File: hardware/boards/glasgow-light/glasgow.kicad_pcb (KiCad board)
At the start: 2 copper layers, 90.2 x 21 mm, 183 parts, among them J1 USB_C_USB2.0, J10 AUX, J2 IDC-Header_2x5_P2.54mm, J3 IDC-Header_2x5_P2.54mm, J4 Conn_01x02, U1 LM358_DFN, U10 SN74LVC1T45DCKR, U11 SN74LVC1T45DCKR, U12 INA180A2, U15 TPD3S014, U16 SN74LVC1T45DCKR, U17 SN74LVC1T45DCKR, U18 SN74LVC1T45DCKR, U19 PCA6408APW, U2 GD32VF103T, U31 TPS73101DBV, U36 TLV73312PQDRVR, U4 SN74LVC1T45DCKR, U5 ICE40UP5K-SG48ITR, U6 SN74LVC1T45DCKR, U8 TLV75533PDRVR, U9 SN74LVC1T45DCKR, Y1 8M

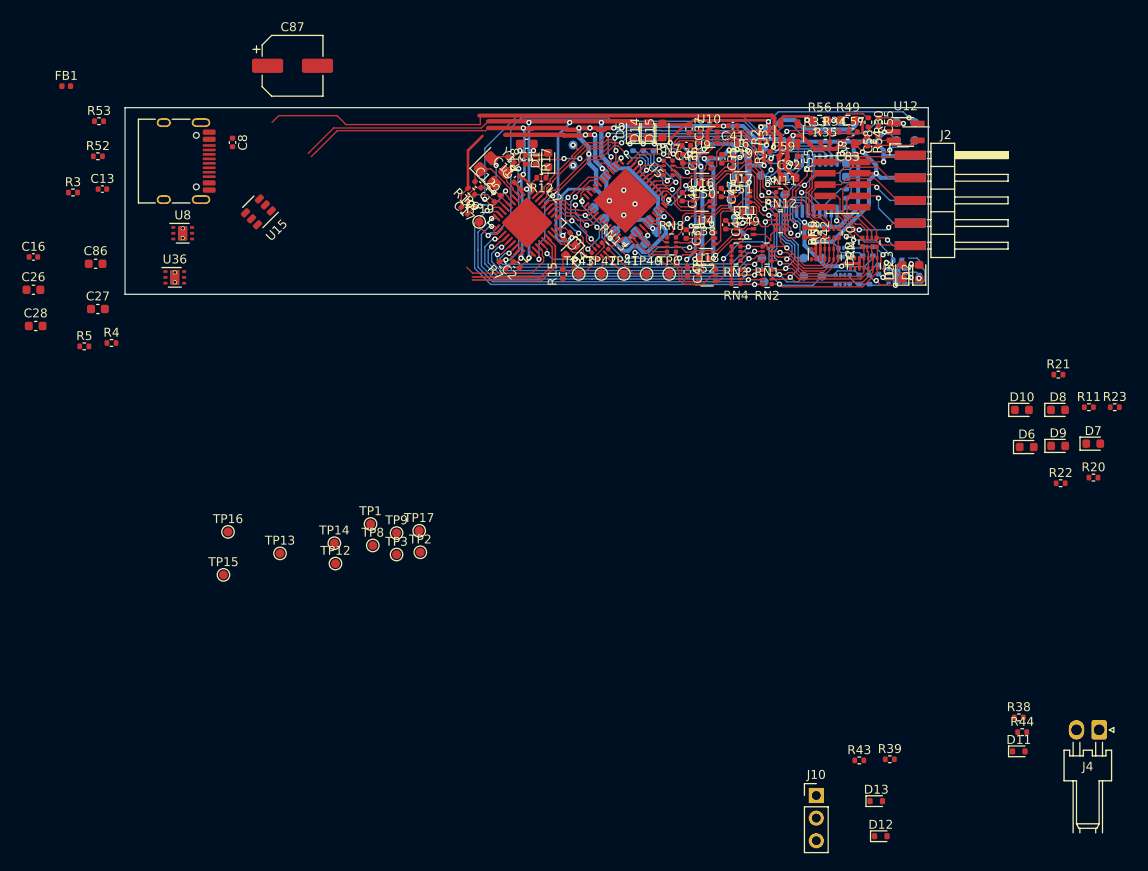
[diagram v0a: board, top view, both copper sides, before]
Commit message: replace SYNC and AUX connectors by test points
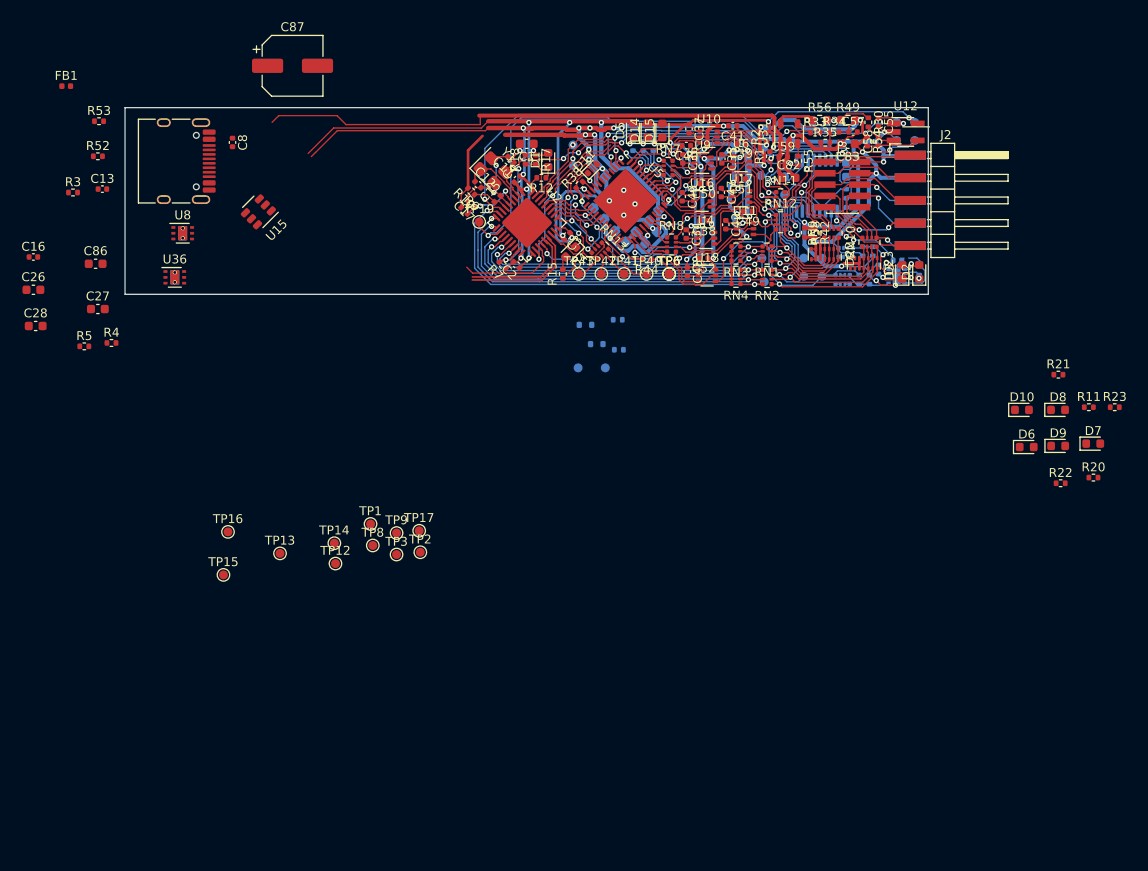
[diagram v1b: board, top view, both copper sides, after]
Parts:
- removed J10: AUX, Connector_PinHeader_2.54mm:PinHeader_1x03_P2.54mm_Vertical
- removed J4: Conn_01x02, Glasgow:Molex_KK-254_1x02_P2.54mm_Horizontal
- added TP18: SYNC, TestPoint:TestPoint_Pad_D1.0mm, B.Cu at (137.7, 62.9)
- added TP6: SYNC, TestPoint:TestPoint_Pad_D1.0mm, F.Cu at (144.9, 52.3)
- added TP7: SYNC, TestPoint:TestPoint_Pad_D1.0mm, B.Cu at (134.7, 62.9)
- D12, D13, R39, R43: moved to B.Cu
- moved D11 81.1 mm to (136.3, 40.5), turned to 45 degrees
- moved R38 77.5 mm to (134.8, 42.3), turned to 45 degrees
- moved R44 67.8 mm to (142.4, 50.7), turned to 180 degrees
- moved D12 66.3 mm to (135.5, 58.0)
- moved D13 60.1 mm to (136.8, 60.2)
- moved R43 56.4 mm to (139.1, 57.5)
- moved R39 55.1 mm to (139.3, 60.8)
- moved D4 0.18 mm to (133.9, 49.9)
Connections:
- R38 pad 2: Net-(R38-Pad2) -> /~SYNC_INT
- R39 pad 2: Net-(R39-Pad2) -> /AUX1
- R43 pad 2: Net-(R43-Pad2) -> /AUX2
- TP6 pad 1: /~SYNC -> /IO_Banks/~SYNC
- U5 pad 10: /~SYNC -> /~SYNC_INT
- U5 pad 11: Net-(U5-Pad11) -> /AUX2
- U5 pad 9: Net-(U5-Pad9) -> /AUX1
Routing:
- net /IO_Banks/~SYNC: track 0.00 -> 20.4 mm, vias 0 -> 2
- net /~SYNC: track 17.6 -> 0.00 mm, vias 2 -> 0
- net +3V3: track 256.5 -> 260.4 mm
- net /~FPGA_RESET: track 12.6 -> 15.7 mm
- net GND: track 337.5 -> 340.4 mm, vias 34 -> 35
- net /FPGA_DONE: track 20.2 -> 22.9 mm
- net Net-(U5-Pad4): track 1.87 -> 0.00 mm
- net /~SYNC_INT: track 0.00 -> 1.33 mm
- net /SCL: track 44.1 -> 45.2 mm
- net /AUX1: track 0.00 -> 1.00 mm, vias 0 -> 1
- net /AUX2: track 0.00 -> 0.78 mm, vias 0 -> 1

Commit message: most components are placed
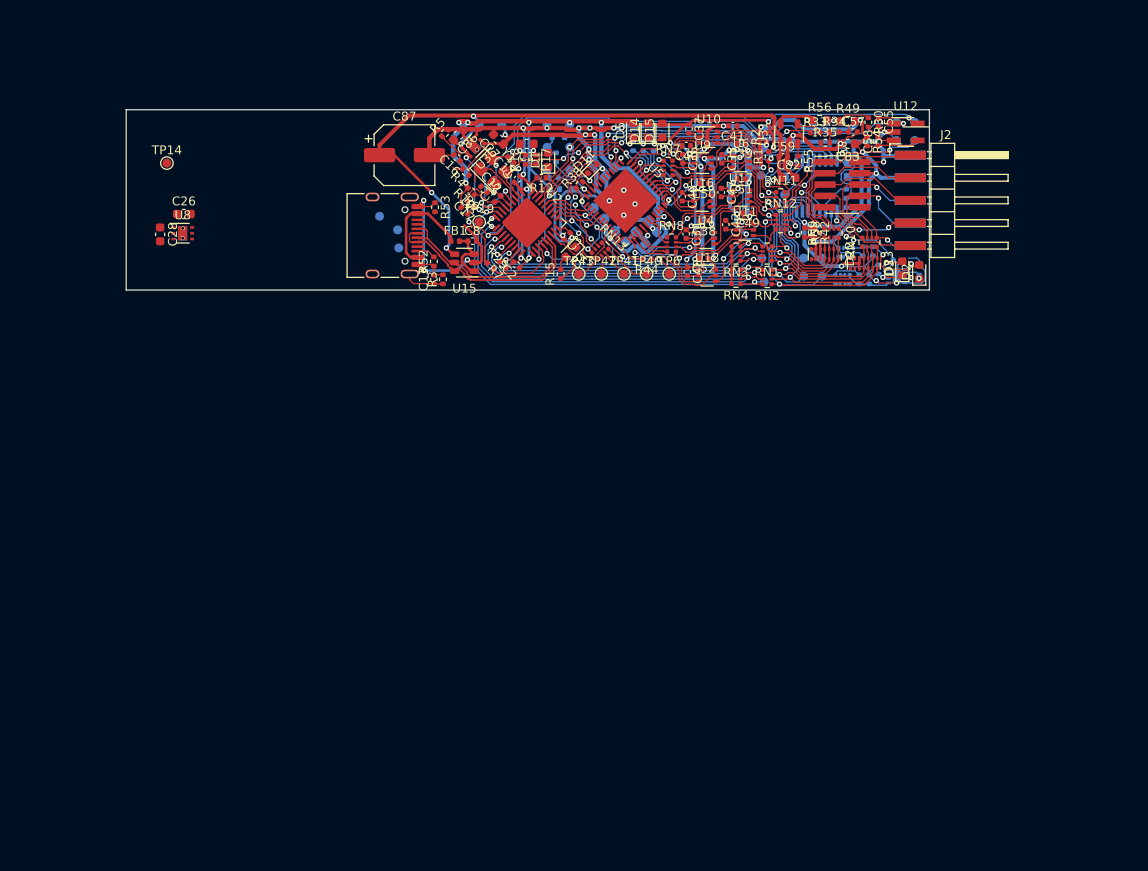
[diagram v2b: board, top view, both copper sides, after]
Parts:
- removed D10, D6: BLU, LED_SMD:LED_0603_1608Metric
- removed D7, D9: PNK, LED_SMD:LED_0603_1608Metric
- removed D8: WHT, LED_SMD:LED_0603_1608Metric
- removed R11, R23: 4k7, Resistor_SMD:R_0402_1005Metric
- removed R20, R22: 10k, Resistor_SMD:R_0402_1005Metric
- removed R21: 6k8, Resistor_SMD:R_0402_1005Metric
- removed TP17: 1V2, TestPoint:TestPoint_Pad_D1.0mm
- removed the TP6 at (144.9, 52.3)
- removed TP8: 5V, TestPoint:TestPoint_Pad_D1.0mm
- removed TP9: 3V3, TestPoint:TestPoint_Pad_D1.0mm
- added R29: 0, Resistor_SMD:R_0402_1005Metric, F.Cu at (124.8, 51.4)
- TP1, TP12, TP13, TP15, TP16, TP2, TP3: moved to B.Cu
- moved TP12 54.7 mm to (131.2, 35.6)
- moved TP3 52.0 mm to (133.7, 35.6)
- moved TP2 48.9 mm to (126.1, 35.6)
- moved C27 48.8 mm to (125.7, 37.2), turned to 135 degrees
- moved C16 48.8 mm to (121.1, 39.3), turned to 135 degrees
- moved R5 47.0 mm to (119.7, 36.5), turned to 45 degrees
- moved FB1 47.0 mm to (120.9, 48.6)
- moved TP14 46.6 mm to (88.5, 39.9)
- moved TP1 46.5 mm to (123.6, 35.6)
- moved R4 44.2 mm to (122.1, 40.9), turned to 135 degrees
- moved TP15 43.4 mm to (114.4, 47.4)
- moved C86 43.2 mm to (121.2, 36.7), turned to 225 degrees
- moved R3 42.7 mm to (119.5, 52.9), turned to 90 degrees
- moved R52 39.5 mm to (118.5, 50.9), turned to 90 degrees
- moved TP13 39.5 mm to (112.4, 45.8)
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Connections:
- net Net-(D12-Pad1) renamed /IO_Banks/AUX1~
- net Net-(D13-Pad1) renamed /IO_Banks/AUX2~
- U2 pad 21: +5V -> Net-(R29-Pad2)
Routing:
- net GND: track 340.4 -> 367.1 mm, vias 35 -> 39
- net +3V3: track 260.4 -> 240.7 mm, vias 23 -> 26
- net +5V: track 77.0 -> 91.2 mm, vias 0 -> 6
- net /xVBUS: track 0.00 -> 12.2 mm
- net /USB_P: track 13.5 -> 24.8 mm
- net +1V2: track 29.5 -> 39.9 mm, vias 4 -> 5
- net /USB_N: track 12.7 -> 22.8 mm
- net Net-(R29-Pad2): track 0.00 -> 8.26 mm
- net /VUSB: track 0.00 -> 6.57 mm
- net Net-(C16-Pad1): track 0.00 -> 5.87 mm
- net /AUX1: track 1.00 -> 5.91 mm
- net /SHLD: track 0.00 -> 4.57 mm
- net /AUX2: track 0.78 -> 4.22 mm
- net /IO_Banks/AUX2~: track 0.00 -> 2.74 mm
- net /IO_Banks/AUX1~: track 0.00 -> 2.66 mm
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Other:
- board size 90.2 x 21 mm -> 90.2 x 20.2 mm

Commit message: optimize
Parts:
- TP14, TP19: moved to B.Cu
- moved C28 34.6 mm to (122.3, 45.3), turned to 225 degrees
- moved U8 31.2 mm to (121.2, 43.2), turned to 225 degrees
- moved C26 30.2 mm to (120.3, 41.1), turned to 225 degrees
- moved TP14 27.7 mm to (116.2, 40.8)
- moved TP13 5.24 mm to (113.7, 40.8)
- moved TP16 4.93 mm to (119.4, 50.4)
- moved TP15 4.22 mm to (118.5, 48.5)
- moved TP19 2.62 mm to (126.0, 47.5)
- moved R9 1.90 mm to (120.8, 46.7)
- moved C17 1.78 mm to (124.0, 45.7), turned to 45 degrees
- moved R10 1.31 mm to (123.7, 43.9)
- moved R4 0.70 mm to (122.6, 41.4)
- moved C16 0.60 mm to (121.6, 39.6)
- moved C12 0.30 mm to (124.3, 43.1)
- moved C13 0.25 mm to (118.5, 52.7)
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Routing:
- net GND: track 367.1 -> 392.5 mm, vias 39 -> 42
- net +5V: track 91.2 -> 98.9 mm, vias 6 -> 7
- net /IO_Banks/VIOA: track 134.9 -> 127.6 mm
- net /xVBUS: track 12.2 -> 18.6 mm, vias 0 -> 1
- net Net-(C16-Pad1): track 5.87 -> 11.8 mm, vias 0 -> 2
- net /CC1: track 0.00 -> 4.19 mm, vias 0 -> 2
- net /USB_N: track 22.8 -> 25.7 mm, vias 0 -> 1
- net /NRST: track 7.06 -> 9.24 mm
- net /USB_P: track 24.8 -> 26.5 mm, vias 0 -> 1
- net +1V2: track 39.9 -> 41.1 mm
- net /VDDA: track 4.11 -> 3.01 mm
- net +3V3: track 240.7 -> 239.7 mm
- net VIO_CURRENT: track 61.4 -> 60.4 mm
- net /XTALIN: track 7.30 -> 7.99 mm
- net VIO_DAC: track 51.9 -> 51.3 mm
- added copper zone on B.Cu, net +5V
- added copper zone on F.Cu, net +5V
- added copper zone on F.Cu, net /SHLD
- added copper zone on B.Cu, net GND
- added copper zone on F.Cu, net GND
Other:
- board size 90.2 x 20.2 mm -> 63.9 x 20.2 mm

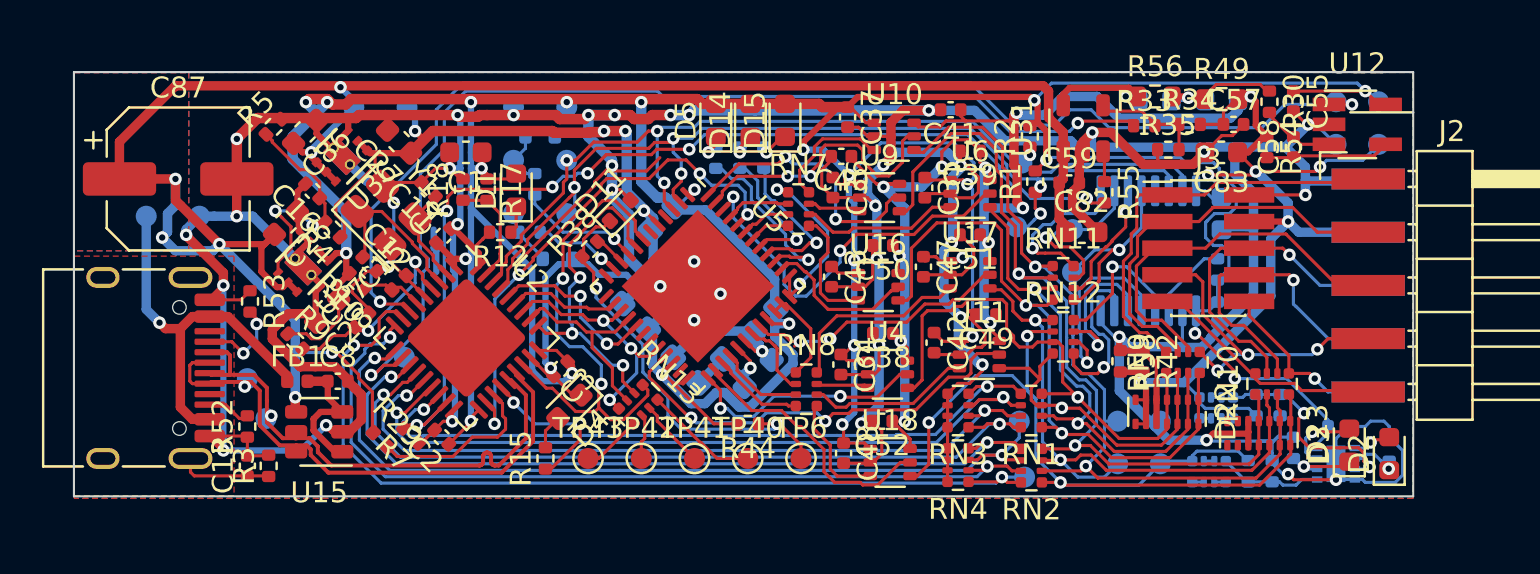
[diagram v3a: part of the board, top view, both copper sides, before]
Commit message: make the board a bit smaller
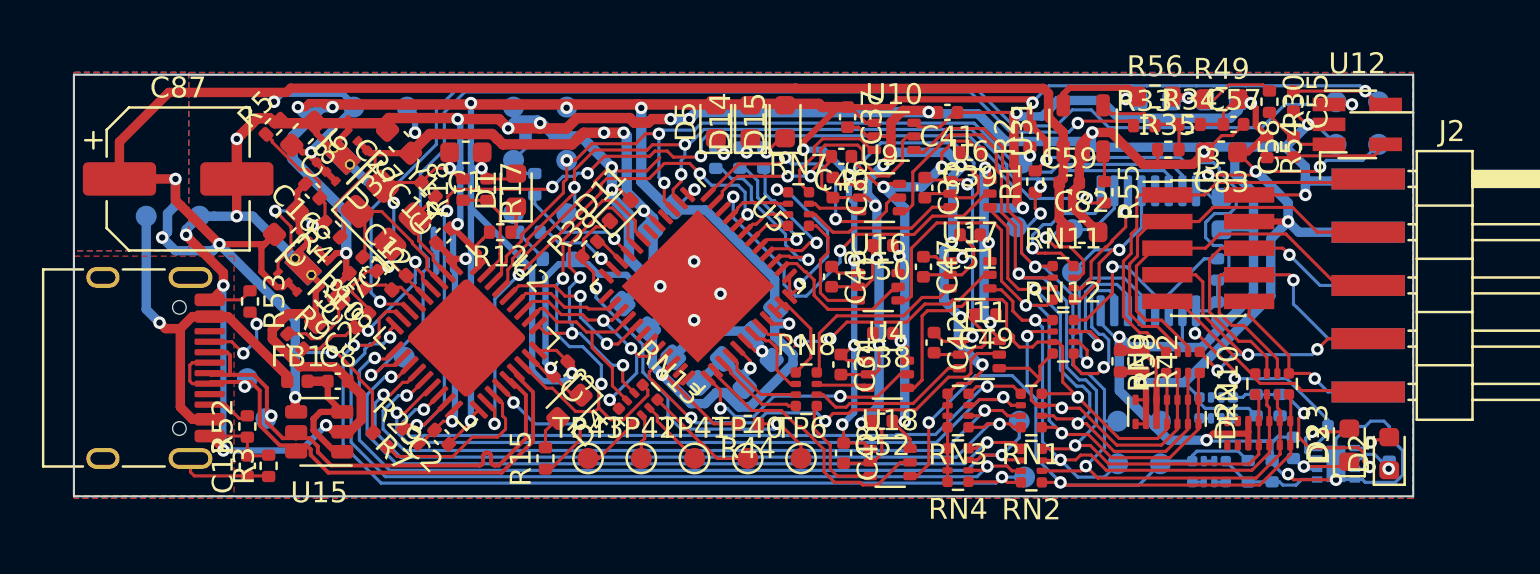
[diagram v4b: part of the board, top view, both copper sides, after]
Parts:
- moved C41 0.20 mm to (151.9, 35.8)
- moved C86 0.12 mm to (121.2, 36.8)
- moved C39 0.06 mm to (153.0, 37.7)
- moved D14 0.06 mm to (142.5, 36.3)
- moved D15 0.06 mm to (144.1, 36.3)
- moved D5 0.06 mm to (140.8, 36.3)
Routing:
- net +5V: track 98.9 -> 102.8 mm
- net GND: track 392.5 -> 389.8 mm, vias 42 -> 41
- net /IO_Banks/VIOA: track 127.6 -> 125.6 mm
- net VIO_ENA: track 48.3 -> 49.0 mm
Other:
- board size 63.9 x 20.2 mm -> 63.9 x 20.1 mm
- rule trace_min: 0.15 -> 0.127

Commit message: make board another bit smaller -> outer size is metric
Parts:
- moved R14 0.18 mm to (167.3, 52.8)
- moved R19 0.13 mm to (168.4, 51.7)
- moved RN2 0.13 mm to (155.9, 52.5)
- moved R25 0.13 mm to (166.2, 52.8)
- moved TP29 0.13 mm to (155.6, 53.1)
- moved RN6 0.12 mm to (164.4, 52.8)
- moved RN4 0.10 mm to (152.4, 52.5)
- moved U18 0.08 mm to (149.2, 52.4)
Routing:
- net GND: track 389.8 -> 388.1 mm
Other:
- board size 63.9 x 20.1 mm -> 64 x 20 mm

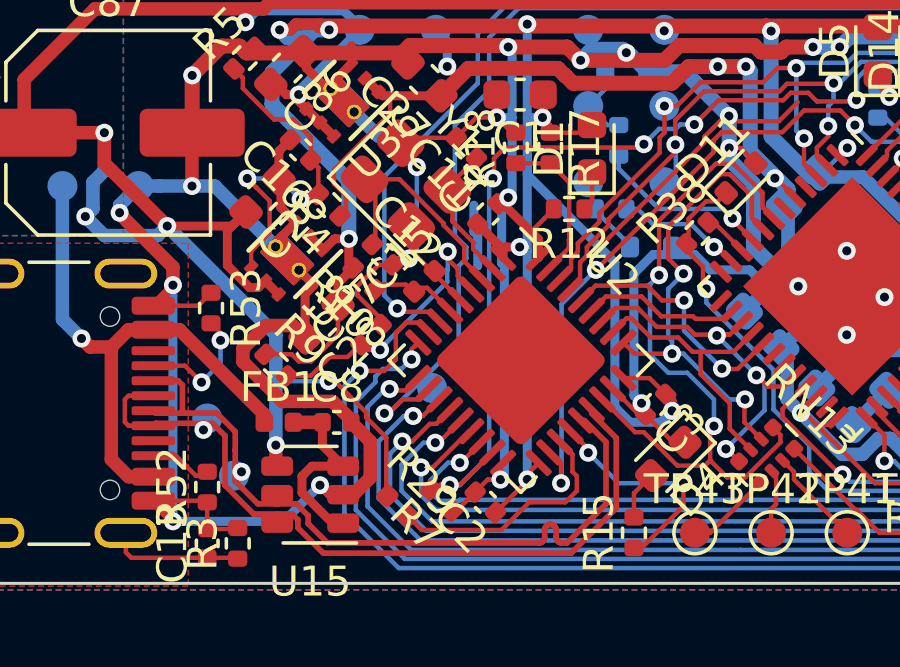
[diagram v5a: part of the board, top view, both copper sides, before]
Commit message: add optional connection for exposed pad of GD32VF
The datasheet doesn't say whether we should connect it to GND.
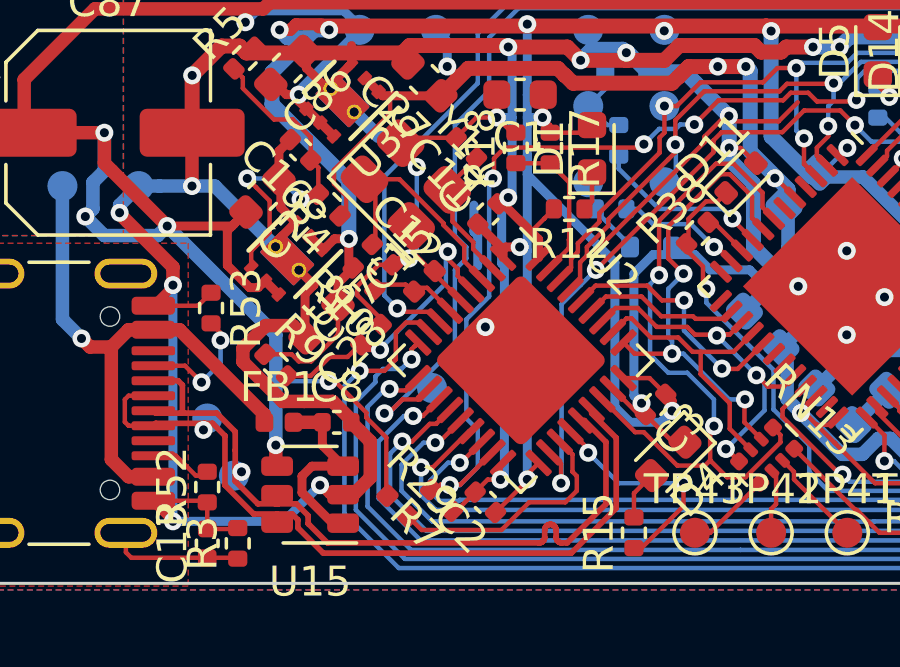
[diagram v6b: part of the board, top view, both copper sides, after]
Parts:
- added R11: 0, Resistor_SMD:R_0402_1005Metric, B.Cu at (127.8, 46.6)
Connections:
- U2 pad 37: (no net) -> Net-(R11-Pad1)
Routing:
- net Net-(R11-Pad1): track 0.00 -> 2.30 mm, vias 0 -> 1
- net GND: track 388.1 -> 388.7 mm

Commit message: optimize
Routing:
- net GND: track 388.7 -> 387.0 mm
- net +3V3: track 239.6 -> 240.7 mm
- net +5V: track 102.8 -> 103.5 mm
